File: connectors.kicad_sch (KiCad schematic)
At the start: 6 parts, among them CN101 JOY1, CN102 HuCARD

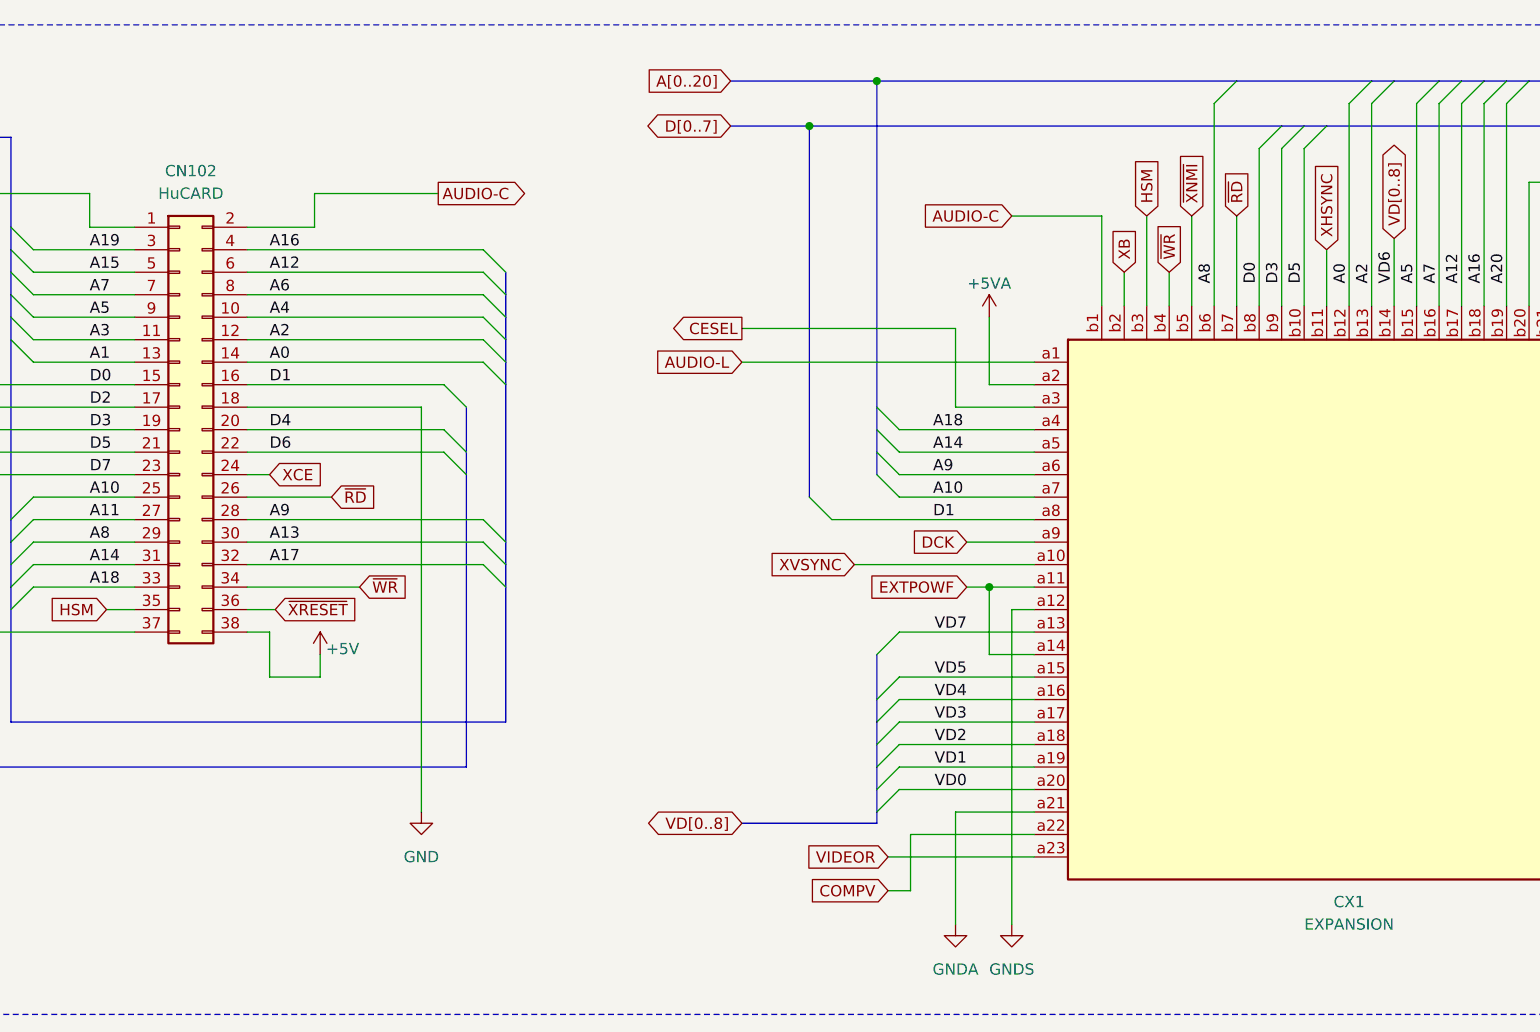
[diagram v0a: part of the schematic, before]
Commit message: Work out numbering of and route some caps.
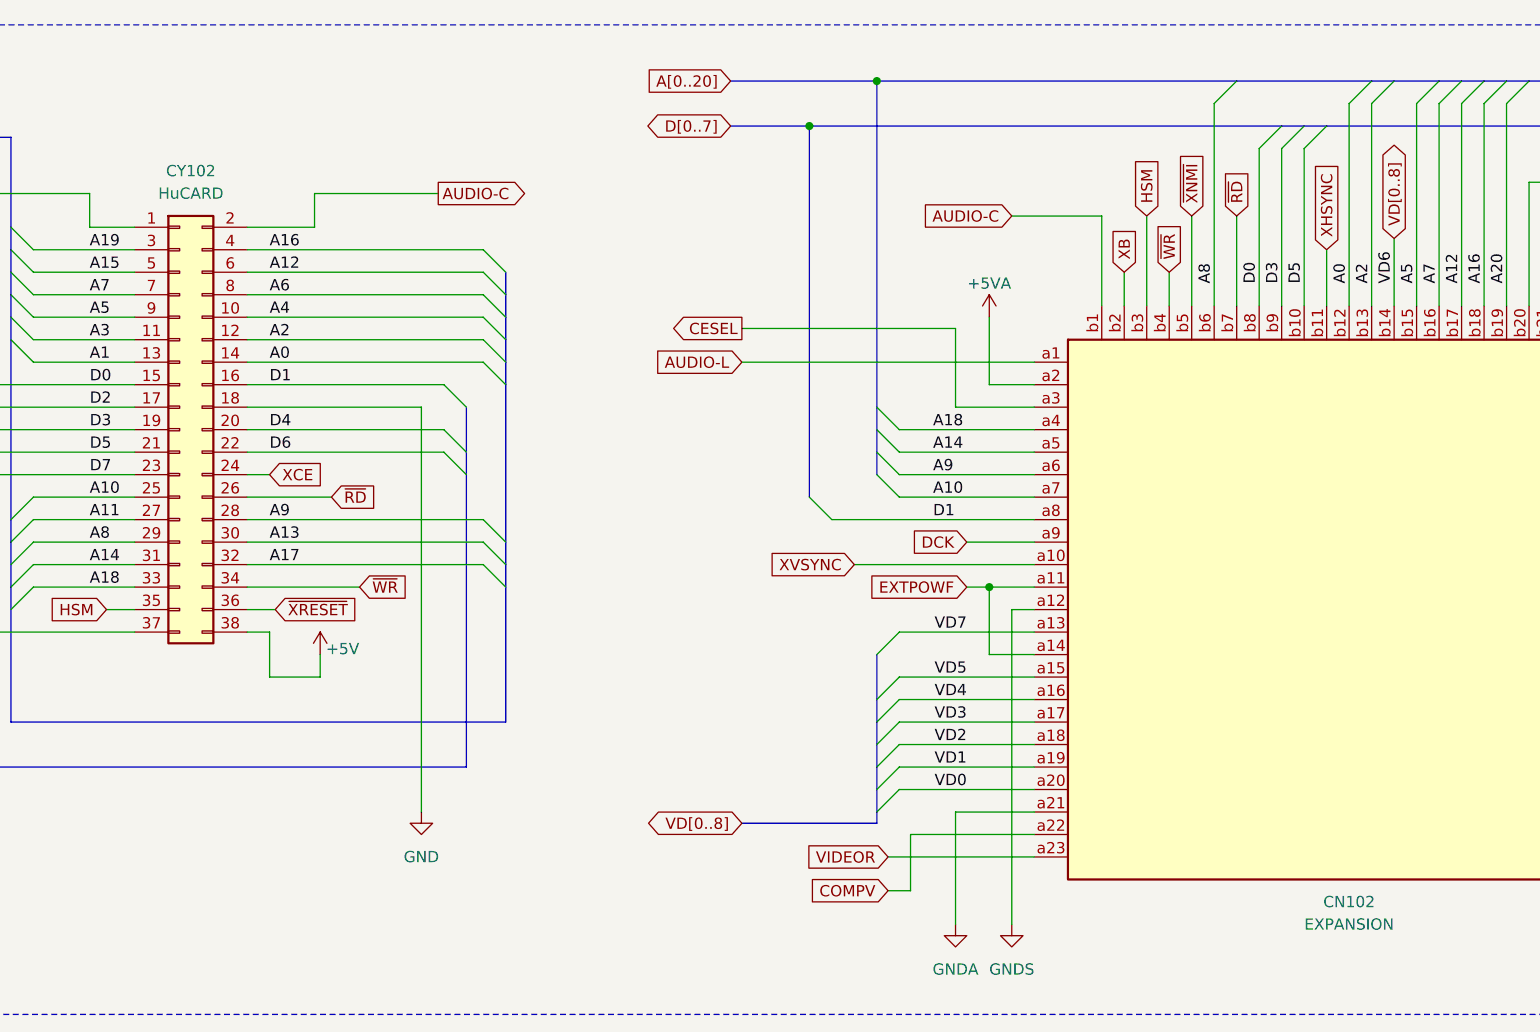
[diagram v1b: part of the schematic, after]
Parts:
- CN102: renamed from CX1; footprint (none) -> A-PCENGINE:CN102-2.54mm
- CX103: now left out of the parts list
- renumbered CN102 to CY102
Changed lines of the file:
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@@
   (symbol (lib_id "Connector_Generic:Conn_02x19_Odd_Even") (at 58.42 176.53 0) (unit 1)
     (in_bom yes) (on_board yes) (dnp no)
-    (property "Reference" "CN102" (at 59.69 147.32 0)
+    (property "Reference" "CY102" (at 59.69 147.32 0)
       (effects (font (size 1.27 1.27)))
     )
@@
       (project "PCE"
         (path "/c1c718c6-a427-431e-a18b-e46f94ae8e09/99dc3156-542f-4db3-aeb5-d38a9dd48b1b"
-          (reference "CN102") (unit 1)
+          (reference "CY102") (unit 1)
         )
       )
@@
   (symbol (lib_id "PC-Engine:Conn_03x23") (at 190.5 196.85 0) (unit 1)
     (in_bom yes) (on_board yes) (dnp no) (fields_autoplaced)
-    (property "Reference" "CX1" (at 190.5 229.87 0)
+    (property "Reference" "CN102" (at 190.5 229.87 0)
       (effects (font (size 1.27 1.27)))
     )
@@
       (effects (font (size 1.27 1.27)))
     )
-    (property "Footprint" "" (at 160.02 196.85 0)
+    (property "Footprint" "A-PCENGINE:CN102-2.54mm" (at 160.02 196.85 0)
       (effects (font (size 1.27 1.27)) hide)
     )
@@
       (project "PCE"
         (path "/c1c718c6-a427-431e-a18b-e46f94ae8e09/99dc3156-542f-4db3-aeb5-d38a9dd48b1b"
-          (reference "CX1") (unit 1)
+          (reference "CN102") (unit 1)
         )
       )
@@
   )
   (symbol (lib_id "PC-Engine:Conn_03x23") (at 189.23 81.28 0) (unit 1)
-    (in_bom yes) (on_board yes) (dnp no) (fields_autoplaced)
+    (in_bom no) (on_board no) (dnp no) (fields_autoplaced)
     (property "Reference" "CX103" (at 189.23 114.3 0)
       (effects (font (size 1.27 1.27)))
@@
       (effects (font (size 1.27 1.27)) hide)
     )
+    (property "Sim.Enable" "0" (at 189.23 81.28 0)
+      (effects (font (size 1.27 1.27)) hide)
+    )

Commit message: Intermediate save
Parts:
- removed CY102: HuCARD, symbol Connector_Generic:Conn_02x19_Odd_Even
- added JP101, JP102: Conn_01x21, A-PCENGINE:JP101-102-2.5mm, symbol Connector_Generic:Conn_01x21
- added L106: ~, A-PCENGINE:L-5.00mm, symbol Device:L
- CN105: renamed from CN101; footprint (none) -> A-PCENGINE:Mini-DIN-8
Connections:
- net +5V: now also JP102.20 (Pin_20)
- net A0: now also JP102.8 (Pin_8)
- net A1: now also JP101.8 (Pin_8)
- net A10: now also JP101.14 (Pin_14)
- net A11: now also JP101.15 (Pin_15)
- net A12: now also JP102.4 (Pin_4)
- net A13: now also JP102.16 (Pin_16)
- net A14: now also JP101.17 (Pin_17)
- net A15: now also JP101.4 (Pin_4)
- net A16: now also JP102.3 (Pin_3)
- net A17: now also JP102.17 (Pin_17)
- net A18: now also JP101.18 (Pin_18)
- net A19: now also JP101.3 (Pin_3)
- net A2: now also JP102.7 (Pin_7)
- net A20: now also JP102.13 (Pin_13)
- net A3: now also JP101.7 (Pin_7)
- net A4: now also JP102.6 (Pin_6)
- net A5: now also JP101.6 (Pin_6)
- net A6: now also JP102.5 (Pin_5)
- net A7: now also JP101.5 (Pin_5)
- net A8: now also JP101.16 (Pin_16)
- net A9: now also JP102.15 (Pin_15)
- net AUDIO-C: now also JP102.2 (Pin_2)
- net D0: now also CN102.c12 (Pin_c12), JP101.9 (Pin_9); no longer CN102.b8 (Pin_b8)
- net D1: now also CN102.c11 (Pin_c11), JP102.9 (Pin_9); no longer CN102.a8 (Pin_a8)
- net D2: now also CN102.b10 (Pin_b10), JP101.10 (Pin_10); no longer CN102.c9 (Pin_c9)
- net D3: now also CN102.c10 (Pin_c10), JP101.11 (Pin_11); no longer CN102.b9 (Pin_b9)
- net D4: now also CN102.b9 (Pin_b9), JP102.11 (Pin_11); no longer CN102.c10 (Pin_c10)
- net D5: now also CN102.c9 (Pin_c9), JP101.12 (Pin_12); no longer CN102.b10 (Pin_b10)
- net D6: now also CN102.a8 (Pin_a8), JP102.12 (Pin_12); no longer CN102.c11 (Pin_c11)
- net D7: now also CN102.b8 (Pin_b8), JP101.13 (Pin_13); no longer CN102.c12 (Pin_c12)
- net GND: now also JP101.1 (Pin_1), JP101.21 (Pin_21), JP102.1 (Pin_1), JP102.21 (Pin_21), L106.2; no longer CN105.8
- net GNDS: no longer CN102.a12 (Pin_a12)
- net HSM: now also JP101.19 (Pin_19)
- net VD[0..8]: no longer CN102.b14 (Pin_b14), CX103.b14 (Pin_b14)
- net XCHECK: now also JP101.2 (Pin_2)
- net ~{RD}: now also JP102.14 (Pin_14)
- net ~{WR}: now also JP102.18 (Pin_18)
- net ~{XIRQ2}: now also JP101.20 (Pin_20)
- net ~{XRESET}: now also JP102.19 (Pin_19)
- new net: CN105.8, L106.1
- new net VD6: CN102.b14 (Pin_b14), CX103.b14 (Pin_b14)
- new net VD8: CN102.a12 (Pin_a12)
- new net ~{CER}: JP102.10 (Pin_10)

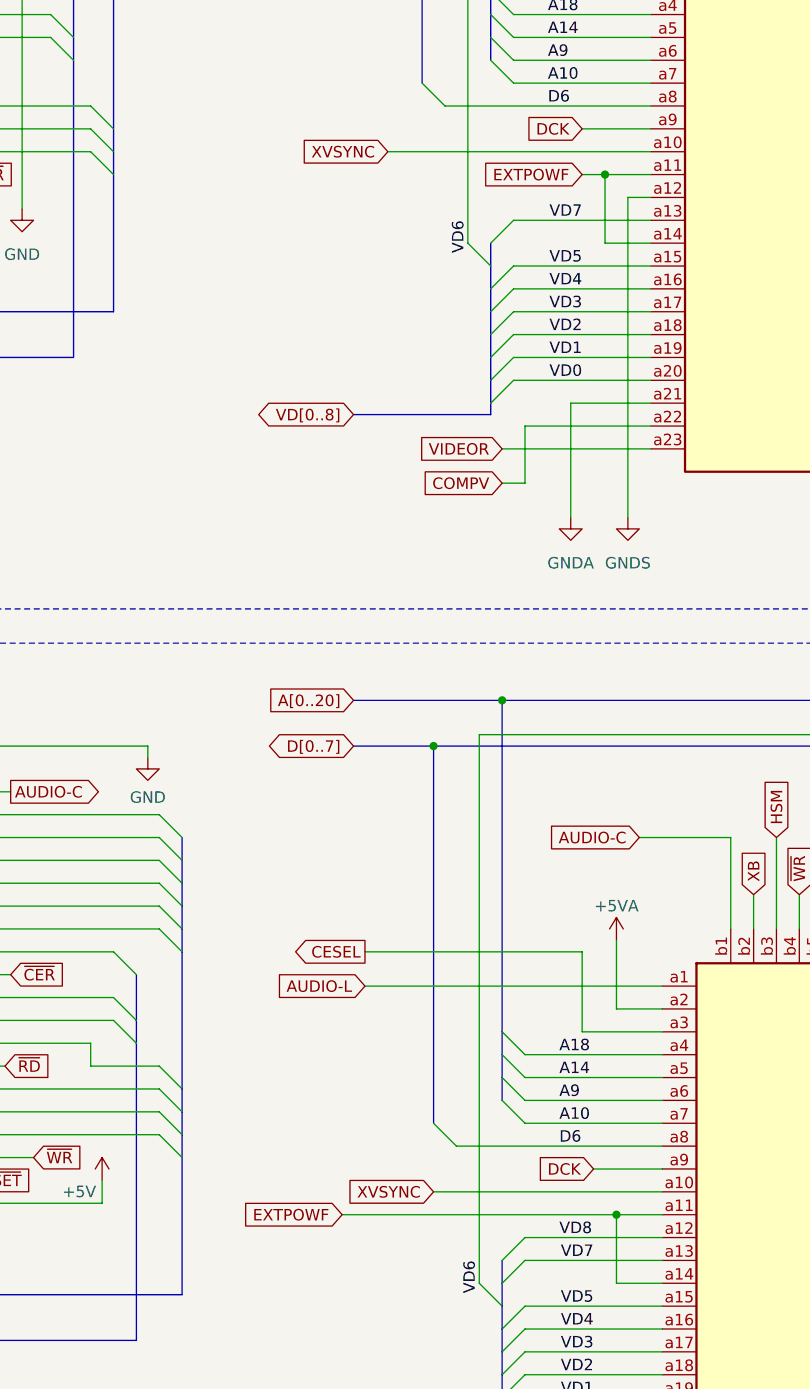
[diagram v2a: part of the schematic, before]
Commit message: Finish basic routing, resolve DRC errors.
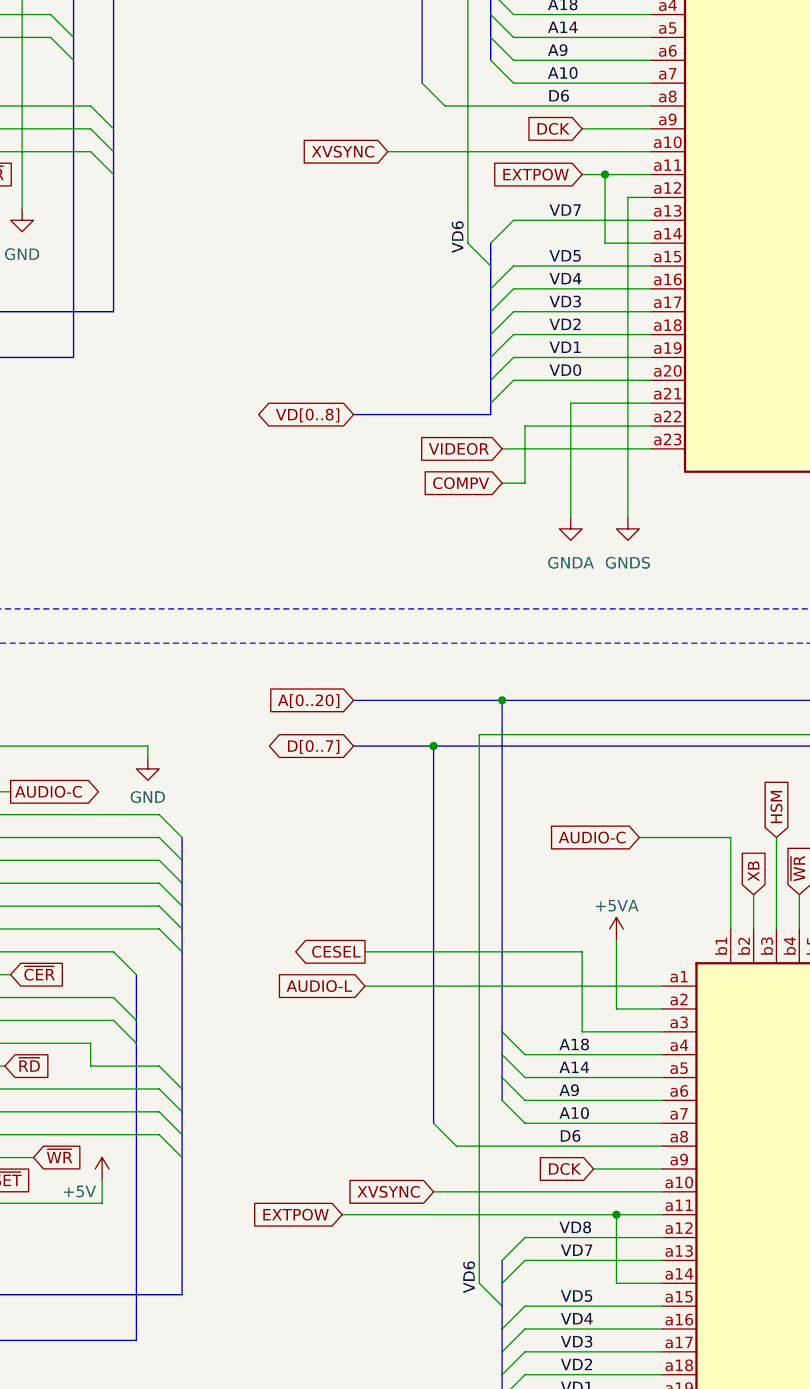
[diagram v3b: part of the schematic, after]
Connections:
- net EXTPOWF renamed EXTPOW
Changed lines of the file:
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@@
     )
   )
-  (global_label "EXTPOWF" (shape input) (at 146.05 78.74 180) (fields_autoplaced)
-    (effects (font (size 1.27 1.27)) (justify right))
-    (property "Intersheetrefs" "${INTERSHEET_REFS}" (at 134.6776 78.74 0)
+  (global_label "EXTPOW" (shape input) (at 146.05 78.74 180) (fields_autoplaced)
+    (effects (font (size 1.27 1.27)) (justify right))
+    (property "Intersheetrefs" "${INTERSHEET_REFS}" (at 135.7662 78.74 0)
       (effects (font (size 1.27 1.27)) (justify right) hide)
     )
@@
     )
   )
-  (global_label "EXTPOWF" (shape input) (at 119.38 194.31 180) (fields_autoplaced)
-    (effects (font (size 1.27 1.27)) (justify right))
-    (property "Intersheetrefs" "${INTERSHEET_REFS}" (at 108.0076 194.31 0)
-      (effects (font (size 1.27 1.27)) (justify right) hide)
-    )
+  (global_label "EXTPOW" (shape input) (at 119.38 194.31 180) (fields_autoplaced)
+    (effects (font (size 1.27 1.27)) (justify right))
+    (property "Intersheetrefs" "${INTERSHEET_REFS}" (at 109.0962 194.31 0)
+      (effects (font (size 1.27 1.27)) (justify right) hide)
+    )

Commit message: First draft of complete PCB.
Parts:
- removed CX101: JOY1, symbol Connector:DIN-8
- removed CX102: HuCARD, symbol Connector_Generic:Conn_02x19_Odd_Even
- removed CX103: EXPANSION, symbol PC-Engine:Conn_03x23
- added CN202: HuCARD, symbol Connector_Generic:Conn_02x19_Odd_Even
- added G1, G2, G3, G4: TestPoint, A-PCENGINE:Grounding_pad, symbol Connector:TestPoint
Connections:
- net +5V: now also CN202.38 (Pin_38)
- net A0: now also CN202.14 (Pin_14)
- net A1: now also CN202.13 (Pin_13)
- net A10: now also CN202.25 (Pin_25)
- net A11: now also CN202.27 (Pin_27)
- net A12: now also CN202.6 (Pin_6)
- net A13: now also CN202.30 (Pin_30)
- net A14: now also CN202.31 (Pin_31)
- net A15: now also CN202.5 (Pin_5)
- net A16: now also CN202.4 (Pin_4)
- net A17: now also CN202.32 (Pin_32)
- net A18: now also CN202.33 (Pin_33)
- net A19: now also CN202.3 (Pin_3)
- net A2: now also CN202.12 (Pin_12)
- net A3: now also CN202.11 (Pin_11)
- net A4: now also CN202.10 (Pin_10)
- net A5: now also CN202.9 (Pin_9)
- net A6: now also CN202.8 (Pin_8)
- net A7: now also CN202.7 (Pin_7)
- net A8: now also CN202.29 (Pin_29)
- net A9: now also CN202.28 (Pin_28)
- net AUDIO-C: now also CN202.2 (Pin_2)
- net D0: now also CN202.15 (Pin_15)
- net D1: now also CN202.16 (Pin_16)
- net D2: now also CN202.17 (Pin_17)
- net D3: now also CN202.19 (Pin_19)
- net D4: now also CN202.20 (Pin_20)
- net D5: now also CN202.21 (Pin_21)
- net D6: now also CN202.22 (Pin_22)
- net D7: now also CN202.23 (Pin_23)
- net GND: now also CN202.18 (Pin_18); no longer CN102.c17 (Pin_c17), CN102.c20 (Pin_c20), CN102.c8 (Pin_c8)
- net HSM: now also CN202.35 (Pin_35)
- net XCE: now also CN202.24 (Pin_24)
- net XCHECK: now also CN202.1 (Pin_1)
- net ~{RD}: now also CN202.26 (Pin_26)
- net ~{WR}: now also CN202.34 (Pin_34)
- net ~{XIRQ2}: now also CN202.37 (Pin_37)
- net ~{XRESET}: now also CN202.36 (Pin_36)
- new net SHIELD: CN102.c17 (Pin_c17), CN102.c20 (Pin_c20), CN102.c8 (Pin_c8)
- no-connect marks 0 -> 4
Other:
- note added: "Mounting hole "decorations""
- note removed: "PCE"
- note removed: "TG16"
- moved on the sheet: CN102, CN105, JP101, JP102, L106
